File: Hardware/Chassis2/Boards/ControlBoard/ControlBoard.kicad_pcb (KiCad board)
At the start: 6 copper layers, 260 x 45 mm, 213 parts, among them IC1 MCP2221A-I_ST, IC2 MAX22530AWE+, IC3 ISO1042BDWVR, IC4 CY15B102Q-SXET, IC6 ISO1042BDWVR, J1 Conn_02x08_Counter_Clockwise, J10 Conn_02x03_Counter_Clockwise, J11 TBP01R2W-508-06BE, J12 Conn_02x08_Counter_Clockwise, J13 Conn_02x03_Counter_Clockwise, J14 Conn_01x10, J15 UJ32-C-H-G-DSMT-3-P24-TR, J2 Conn_01x02, J3 22-04-1041, J5 TBP02R2W-381-08BE, J6 22-04-1041, J7 Conn_02x08_Counter_Clockwise, J8 22-04-1041, J9 22-04-1041, U1 STM32H723ZGTx, U2 ISO1212, U3 LT3080xQ, U4 ISO1212, U5 ISO1212, U6 ISO1212, U7 BTS462TATMA1, U8 BTS462TATMA1, Y1 8MHz

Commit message: eod 2026-07-08
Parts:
- removed C1: ADCM-S05R5SA224XB, InverterCom:ADCMS05R5SA224XB
- removed C6: 100nF, Capacitor_SMD:C_1210_3225Metric_Pad1.33x2.70mm_HandSolder
- removed C7: 1uF, Capacitor_SMD:C_1210_3225Metric_Pad1.33x2.70mm_HandSolder
- removed IC1: MCP2221A-I_ST, InverterCom:SOP65P640X120-14N
- removed J15: UJ32-C-H-G-DSMT-3-P24-TR, InverterCom:UJ32CHGDSMT3P24TR
- removed JP1: Jumper_2_Small_Bridged, Jumper:SolderJumper-2_P1.3mm_Bridged_Pad1.0x1.5mm
- removed JP2: Jumper_2_Small_Open, Jumper:SolderJumper-2_P1.3mm_Open_RoundedPad1.0x1.5mm
- removed R13, R29, R30: 10k, Resistor_SMD:R_1210_3225Metric_Pad1.30x2.65mm_HandSolder
- removed R32, R33: 22, Resistor_SMD:R_1210_3225Metric_Pad1.30x2.65mm_HandSolder
- removed R34, R35, R36, R71, R72: 4.7k, Resistor_SMD:R_1210_3225Metric_Pad1.30x2.65mm_HandSolder
- removed TP24, TP25, TP26: TestPoint, TestPoint:TestPoint_Loop_D2.54mm_Drill1.5mm_Beaded
- added C147: 1uF, Capacitor_SMD:C_1210_3225Metric_Pad1.33x2.70mm_HandSolder, B.Cu at (100.5, 18.0)
- added C149: 100nF, Capacitor_SMD:C_1210_3225Metric_Pad1.33x2.70mm_HandSolder, B.Cu at (100.5, 25.0)
- added C197: 100nF, Capacitor_SMD:C_1210_3225Metric_Pad1.33x2.70mm_HandSolder, B.Cu at (105.5, 18.0)
- added C198: 10uF, Capacitor_SMD:C_1210_3225Metric_Pad1.33x2.70mm_HandSolder, B.Cu at (100.5, 21.5)
- added C200: 1uF, Capacitor_SMD:C_1210_3225Metric_Pad1.33x2.70mm_HandSolder, B.Cu at (105.5, 25.0)
- added C201: 100nF, Capacitor_SMD:C_1210_3225Metric_Pad1.33x2.70mm_HandSolder, B.Cu at (105.5, 21.5)
- added C202: 100nF, Capacitor_SMD:C_1210_3225Metric_Pad1.33x2.70mm_HandSolder, B.Cu at (135.0, 43.0)
- added C203: 100nF, Capacitor_SMD:C_1210_3225Metric_Pad1.33x2.70mm_HandSolder, B.Cu at (123.4, 43.0)
- added C208: 10uF, Capacitor_SMD:C_1210_3225Metric_Pad1.33x2.70mm_HandSolder, B.Cu at (146.9, 8.50)
- added C209: 10uF, Capacitor_SMD:C_1210_3225Metric_Pad1.33x2.70mm_HandSolder, B.Cu at (156.5, 9.56)
- added C210: 10uF, Capacitor_SMD:C_1210_3225Metric_Pad1.33x2.70mm_HandSolder, B.Cu at (166.4, 8.50)
- added C27: 100nF, Capacitor_SMD:C_1210_3225Metric_Pad1.33x2.70mm_HandSolder, B.Cu at (129.5, 39.5)
- added C28: 100nF, Capacitor_SMD:C_1210_3225Metric_Pad1.33x2.70mm_HandSolder, B.Cu at (141.5, 43.0)
- added C33: 22pF, Capacitor_SMD:C_1210_3225Metric_Pad1.33x2.70mm_HandSolder, B.Cu at (108.5, 6.00)
- added C48: 22pF, Capacitor_SMD:C_1210_3225Metric_Pad1.33x2.70mm_HandSolder, B.Cu at (103.5, 6.00)
- added IC5: ISO1042BDWVR, InverterCom:SOIC127P1150X280-8N, B.Cu at (65.0, 32.5)
- added IC7: ISO1042BDWVR, InverterCom:SOIC127P1150X280-8N, B.Cu at (65.5, 14.0)
- added J4: B2B-XH-AM_LF__SN_, InverterCom:B2BXHAMLFSN, F.Cu at (157.8, 3.98)
- added R87: 1k, Resistor_SMD:R_1210_3225Metric_Pad1.30x2.65mm_HandSolder, B.Cu at (220.6, 2.25)
- added R88: 10k, Resistor_SMD:R_1210_3225Metric_Pad1.30x2.65mm_HandSolder, B.Cu at (135.0, 39.5)
- added R89: 10k, Resistor_SMD:R_1210_3225Metric_Pad1.30x2.65mm_HandSolder, B.Cu at (123.5, 39.5)
- added R90: 10k, Resistor_SMD:R_1210_3225Metric_Pad1.30x2.65mm_HandSolder, B.Cu at (153.5, 3.00)
- added R91: 1k, Resistor_SMD:R_1210_3225Metric_Pad1.30x2.65mm_HandSolder, B.Cu at (152.0, 7.50)
- added R92: 10k, Resistor_SMD:R_1210_3225Metric_Pad1.30x2.65mm_HandSolder, B.Cu at (163.0, 3.05)
- added R93: 1k, Resistor_SMD:R_1210_3225Metric_Pad1.30x2.65mm_HandSolder, B.Cu at (161.0, 7.50)
- added R94: 10k, Resistor_SMD:R_1210_3225Metric_Pad1.30x2.65mm_HandSolder, B.Cu at (172.5, 3.00)
- added R95: 1k, Resistor_SMD:R_1210_3225Metric_Pad1.30x2.65mm_HandSolder, B.Cu at (171.6, 7.50)
- added U9: STM32G474RCTx, Package_QFP:LQFP-64_10x10mm_P0.5mm, F.Cu at (102.8, 21.7)
- added Y2: 8MHz, Crystal:Crystal_HC49-4H_Vertical, F.Cu at (108.4, 10.0)
- added Z5: MM3Z3V0ST1G, InverterCom:SOD2512X100N, B.Cu at (149.5, 1.50)
- added Z6: MM3Z3V0ST1G, InverterCom:SOD2512X100N, B.Cu at (159.0, 1.50)
- added Z7: MM3Z3V0ST1G, InverterCom:SOD2512X100N, B.Cu at (168.5, 1.50)
- J1: value Conn_02x08_Counter_Clockwise -> B2B-XH-AM_LF__SN_; footprint Connector_PinHeader_2.54mm:PinHeader_2x08_P2.54mm_Vertical -> InverterCom:B2BXHAMLFSN
- J14: value Conn_01x10 -> Conn_02x08_Counter_Clockwise; footprint Connector_PinHeader_2.54mm:PinHeader_1x10_P2.54mm_Vertical -> Connector_PinHeader_2.54mm:PinHeader_2x08_P2.54mm_Vertical
- J2: value Conn_01x02 -> Conn_02x10_Counter_Clockwise; footprint Connector_PinHeader_2.54mm:PinHeader_1x02_P2.54mm_Vertical -> Connector_PinSocket_2.54mm:PinSocket_2x10_P2.54mm_Vertical
- J5: value TBP02R2W-381-08BE -> B2B-XH-AM_LF__SN_; footprint InverterCom:TBP02R2W38108BE -> InverterCom:B2BXHAMLFSN
- R31: moved to B.Cu
- U3: footprint Package_TO_SOT_SMD:TO-263-5_TabPin3 -> Package_TO_SOT_SMD:TO-263-5_TabPin6
- moved J2 151.1 mm to (95.4, 40.0), turned to 90 degrees
- moved C30 66.5 mm to (118.0, 3.25), turned to 180 degrees
- moved J5 66.2 mm to (167.2, 3.98), turned to 180 degrees
- moved C192 53.3 mm to (123.7, 15.8), turned to 90 degrees
- moved Y1 52.6 mm to (126.2, 4.50), turned to 180 degrees
- moved C26 51.5 mm to (129.5, 2.50), turned to 0 degrees
- moved C184 50.5 mm to (124.4, 30.6)
- moved IC4 49.3 mm to (137.8, 3.37), turned to 180 degrees
- moved C135 49.0 mm to (129.5, 20.0)
- moved C194 45.0 mm to (135.9, 29.6), turned to -90 degrees
- moved J1 44.8 mm to (148.2, 3.98), turned to 180 degrees
- moved C182 43.8 mm to (124.4, 27.1), turned to 180 degrees
- moved C134 43.7 mm to (124.3, 23.6), turned to 0 degrees
- moved LED2 43.4 mm to (146.5, 42.5), turned to 90 degrees
- moved C136 43.1 mm to (128.7, 24.2), turned to 90 degrees
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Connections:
- net /ADC/SPI_RX_A renamed /ADC/SPI_MISO_A
- net /ADC/SPI_TX_A renamed /ADC/SPI_MOSI_A
- net /CAN Transciever/CAN_RX renamed /CAN Transciever/A_CAN_RX
- net /CAN Transciever/CAN_TX renamed /CAN Transciever/A_CAN_TX
- net /CAN Transciever1/CAN_RX renamed /CAN Transciever1/A_CAN_RX
- net /CAN Transciever1/CAN_TX renamed /CAN Transciever1/A_CAN_TX
- net /Control/DC_LINK_CURRENT_SENSE renamed /Control/SN_CUR_SENSE_DC_LINK_SIG
- net /Control/DC_LINK_CURRENT_SENSE_REF renamed /Control/SN_CUR_SENSE_DC_LINK_REF
- net /Control/DEBUG_NJTRST renamed /Control/MP_DEBUG_NJTRST
- net /Control/DEBUG_TRGIO renamed /Control/MP_DEBUG_TRGIO
- net /Control/FRAM_CS renamed /Control/Main Processor/FRAM_CS
- net /Control/FRAM_HOLD renamed /Control/Main Processor/FRAM_HOLD
- net /Control/FRAM_SPI_MISO renamed /Control/Main Processor/FRAM_SPI_MISO
- net /Control/FRAM_SPI_MOSI renamed /Control/Main Processor/FRAM_SPI_MOSI
- net /Control/FRAM_SPI_SCK renamed /Control/Main Processor/FRAM_SPI_SCK
- net /Control/FRAM_WP renamed /Control/Main Processor/FRAM_WP
- net /Control/HALL_U_ENCODER_SIN renamed /Control/SN_HALL_U_ENCODER_SIN
- net /Control/HALL_V_ENCODER_COS renamed /Control/SN_HALL_V_ENCODER_COS
- net /Control/HALL_W renamed /Control/SN_HALL_W
- net /Control/MOTOR_TEMP renamed /Control/SN_MOTOR_TEMP
- net /Control/PHASE_U_CURRENT_SENSE renamed /Control/SN_CUR_SENSE_PH_U_SIG
- net /Control/PHASE_U_CURRENT_SENSE_REF renamed /Control/SN_CUR_SENSE_PH_U_REF
- net /Control/PHASE_V_CURRENT_SENSE renamed /Control/SN_CUR_SENSE_PH_V_SIG
- net /Control/PHASE_V_CURRENT_SENSE_REF renamed /Control/SN_CUR_SENSE_PH_V_REF
- net /Control/PHASE_W_CURRENT_SENSE renamed /Control/SN_CUR_SENSE_PH_W_SIG
- net /Control/PHASE_W_CURRENT_SENSE_REF renamed /Control/SN_CUR_SENSE_PH_W_REF
- net /Control/THROTTLE_A renamed /Control/SN_THROTTLE_A
- net /Control/USER_DIN_1 renamed /Control/SN_USER_DIN_1
- net /Control/USER_DIN_2 renamed /Control/SN_USER_DIN_2
- net /Control/USER_DIN_3 renamed /Control/SN_USER_DIN_3
- net /Control/USER_DIN_4 renamed /Control/SN_USER_DIN_4
- net /Control/USER_DIN_5 renamed /Control/MP_USER_DIN_5
- net /Control/USER_DIN_6 renamed /Control/MP_USER_DIN_6
- net /Control/USER_DIN_7 renamed /Control/MP_USER_DIN_7
- net /Control/USER_DIN_8 renamed /Control/MP_USER_DIN_8
- net /SWCLK renamed /MP_SWCLK
- net /VSENSE_DC_LINK_Y renamed /VS_DC_LINK_Y
- net /VSENSE_GND_Y renamed /VS_GND_Y
- net /VSENSE_PH_U_Y renamed /VS_PH_U_Y
- net /VSENSE_PH_V_Y renamed /VS_PH_V_Y
- net /VSENSE_PH_W_Y renamed /VS_PH_W_Y
- net Net-(IC3-CANH) renamed /CAN Transciever1/CAN_H
- net Net-(IC3-CANL) renamed /CAN Transciever1/CAN_L
- net Net-(IC6-CANH) renamed /CAN Transciever/CAN_H
- net Net-(IC6-CANL) renamed /CAN Transciever/CAN_L
- C134 pad 1: Net-(C1-+) -> /+3.3V_A
- C135 pad 1: /+3.3V_A -> /GND_A
- C135 pad 2: Net-(U1-VDDA) -> /+3.3V_A
- C136 pad 1: /+3.3V_A -> /GND_A
- C136 pad 2: Net-(U1-VDDA) -> /+3.3V_A
- C140 pad 2: /ANALOG_GND -> /GND_A
- C141 pad 2: /ANALOG_GND -> /GND_A
- C142 pad 1: /ANALOG_GND -> /GND_A
- C143 pad 2: /ANALOG_GND -> /GND_A
- C144 pad 2: /ANALOG_GND -> /GND_A
- C145 pad 2: /ANALOG_GND -> /GND_A
- C146 pad 2: /ANALOG_GND -> /GND_A
- C190 pad 2: /GND_A -> Net-(C190-Pad2)
- C191 pad 2: /GND_A -> Net-(C190-Pad2)
- C192 pad 1: Net-(U1-VREF+) -> /+3.3V_A
- C193 pad 1: Net-(U1-VREF+) -> /+3.3V_A
- C21 pad 2: /ANALOG_GND -> /GND_A
- C22 pad 2: /ANALOG_GND -> /GND_A
- C23 pad 2: /ANALOG_GND -> /GND_A
- C24 pad 2: /ANALOG_GND -> /GND_A
- C25 pad 2: /ANALOG_GND -> /GND_A
- C29 pad 2: /ANALOG_GND -> /GND_A
- C38 pad 2: /ANALOG_GND -> /GND_A
- C39 pad 2: /ANALOG_GND -> /GND_A
- C42 pad 2: /ANALOG_GND -> /GND_A
- C43 pad 2: /ANALOG_GND -> /GND_A
- C44 pad 2: /ANALOG_GND -> /GND_A
- C45 pad 1: /Control/THROTTLE_B -> /Control/SN_THROTTLE_B
- C45 pad 2: /ANALOG_GND -> /GND_A
- C46 pad 2: /ANALOG_GND -> /GND_A
- C47 pad 2: /ANALOG_GND -> /GND_A
- J1 pad 2: /FAULT -> Net-(Z5-K)
- J14 pad 1: /+3.3V_A -> /GND_A
- J14 pad 10: /RESET -> /+3.3V_A
- J14 pad 2: /SWDIO -> /MP_SWO
- J14 pad 3: /GND_A -> /MP_BOOTSEL
- J14 pad 5: /GND_A -> /MP_SWDIO
- J14 pad 6: /SWO -> /MP_RESET
- J14 pad 7: unconnected-(J14-Pin_7-Pad7) -> /GND_A
- J14 pad 8: unconnected-(J14-Pin_8-Pad8) -> /USB_DP
- J14 pad 9: /GND_A -> /USB_DM
- J2 pad 1: /+12V_A -> /GND_A
- J2 pad 2: /GND_A -> /FAULT
- J3 pad 3: /ANALOG_GND -> /GND_A
- J5 pad 1: /+3.3V_A -> /GND_A
- J5 pad 2: /HS_TMP_2 -> Net-(Z7-K)
- J6 pad 3: /ANALOG_GND -> /GND_A
- J8 pad 3: /ANALOG_GND -> /GND_A
- J9 pad 3: /ANALOG_GND -> /GND_A
- R14 pad 1: /BOOTSEL -> /MP_BOOTSEL
- R40 pad 1: /ANALOG_GND -> /GND_A
- R42 pad 1: /ANALOG_GND -> /GND_A
- R44 pad 1: /ANALOG_GND -> /GND_A
- R46 pad 1: /ANALOG_GND -> /GND_A
- R48 pad 1: /ANALOG_GND -> /GND_A
- R50 pad 1: /ANALOG_GND -> /GND_A
- R52 pad 1: /ANALOG_GND -> /GND_A
- R54 pad 1: /ANALOG_GND -> /GND_A
- R56 pad 1: /ANALOG_GND -> /GND_A
- R58 pad 1: /ANALOG_GND -> /GND_A
- R60 pad 1: /ANALOG_GND -> /GND_A
- R61 pad 1: /Control/THROTTLE_B -> /Control/SN_THROTTLE_B
- R62 pad 1: /ANALOG_GND -> /GND_A
- R62 pad 2: /Control/THROTTLE_B -> /Control/SN_THROTTLE_B
- R64 pad 1: /ANALOG_GND -> /GND_A
- R66 pad 1: /ANALOG_GND -> /GND_A
- R70 pad 1: /RESET -> /MP_RESET
- R86 pad 1: /ANALOG_GND -> /GND_A
- S1 pad 3: /BOOTSEL -> /MP_BOOTSEL
- S1 pad 4: /BOOTSEL -> /CP_BOOTSEL
- S2 pad 3: /RESET -> /MP_RESET
- S2 pad 4: /RESET -> /CP_RESET
- U1 pad 105: /SWDIO -> /MP_SWDIO
- U1 pad 111: /GATE_DRIVE_PWR_ENABLE -> /GATE_DRIVE_PWR1_ENABLE
- U1 pad 117: unconnected-(U1-PD3-Pad117) -> /GATE_DRIVE_PWR2_FB
- U1 pad 118: unconnected-(U1-PD4-Pad118) -> /GATE_DRIVE_PWR1_FB
- U1 pad 133: /SWO -> /MP_SWO
- U1 pad 138: /BOOTSEL -> /MP_BOOTSEL
- U1 pad 18: unconnected-(U1-PF6-Pad18) -> /Control/SN_THROTTLE_B
- U1 pad 20: unconnected-(U1-PF8-Pad20) -> /HS_TMP_1
- U1 pad 25: /RESET -> /MP_RESET
- U1 pad 31: /ANALOG_GND -> /GND_A
- U1 pad 32: Net-(U1-VREF+) -> /+3.3V_A
- U1 pad 33: Net-(U1-VDDA) -> /+3.3V_A
- U1 pad 40: /Control/THROTTLE_B -> /Control/PHASE_CURSENSE_COMP_N
- U1 pad 41: /HS_TMP_1 -> /Control/DC_LINK_CURSENSE_COMP_N
- U1 pad 6: Net-(C1-+) -> /+3.3V_A
- U1 pad 69: /Control/USART3_TX -> /Control/Main Processor/USART3_TX
- U1 pad 70: /Control/USART3_RX -> /Control/Main Processor/USART3_RX
- U1 pad 77: unconnected-(U1-PD8-Pad77) -> /Control/Main Processor/COPROCESSOR_SYNC
- U1 pad 78: unconnected-(U1-PD9-Pad78) -> /Control/Main Processor/COPROCESSOR_WAKEUP
- U1 pad 79: unconnected-(U1-PD10-Pad79) -> /CP_RESET
- U1 pad 80: unconnected-(U1-PD11-Pad80) -> /CP_BOOTSEL
- U1 pad 96: unconnected-(U1-PC6-Pad96) -> /Control/Main Processor/COPROCESSOR_TIMER_SYNC_OUT
- U3 pad 5: Net-(U3-IN) -> /+12V_SWITCHED_A
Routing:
- net /ANALOG_GND: track 127.5 -> 0.00 mm, vias 13 -> 0
- net /RESET: track 120.4 -> 0.00 mm, vias 7 -> 0
- net /CAN Transciever1/A_CAN_TX: track 116.3 -> 22.0 mm, vias 2 -> 0
- net /ADC/ADC1_CS_A: track 122.0 -> 31.1 mm, vias 2 -> 0
- net /BOOTSEL: track 90.5 -> 0.00 mm, vias 5 -> 0
- net /ADC/ADC1_INT_A: track 121.4 -> 31.1 mm, vias 2 -> 0
- net /FAULT: track 90.1 -> 0.00 mm, vias 4 -> 0
- net /CAN Transciever/A_CAN_TX: track 100.4 -> 20.1 mm, vias 2 -> 0
- net /CAN Transciever1/A_CAN_RX: track 103.9 -> 23.9 mm, vias 4 -> 0
- net /CAN Transciever/A_CAN_RX: track 97.8 -> 18.4 mm, vias 2 -> 0
- net /Control/USART3_TX: track 75.2 -> 0.00 mm, vias 2 -> 0
- net /ADC/SPI_MISO_A: track 104.8 -> 31.9 mm, vias 2 -> 0
- net /ADC/SPI_MOSI_A: track 103.5 -> 31.4 mm, vias 2 -> 0
- net /Control/SN_USER_DIN_1: track 105.2 -> 33.3 mm, vias 3 -> 0
- net /Control/USART3_RX: track 71.3 -> 0.00 mm, vias 2 -> 0
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- removed copper zone on B.Cu, net /ANALOG_GND
- removed copper zone on F.Cu, net /ANALOG_GND
- removed copper zone on In1.Cu, net /ANALOG_GND
- removed copper zone on In4.Cu, net /ANALOG_GND
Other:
- board text removed: "3.3V|TMP2|3.3V|TMP3|GND|3.3V|TMP1|GND"

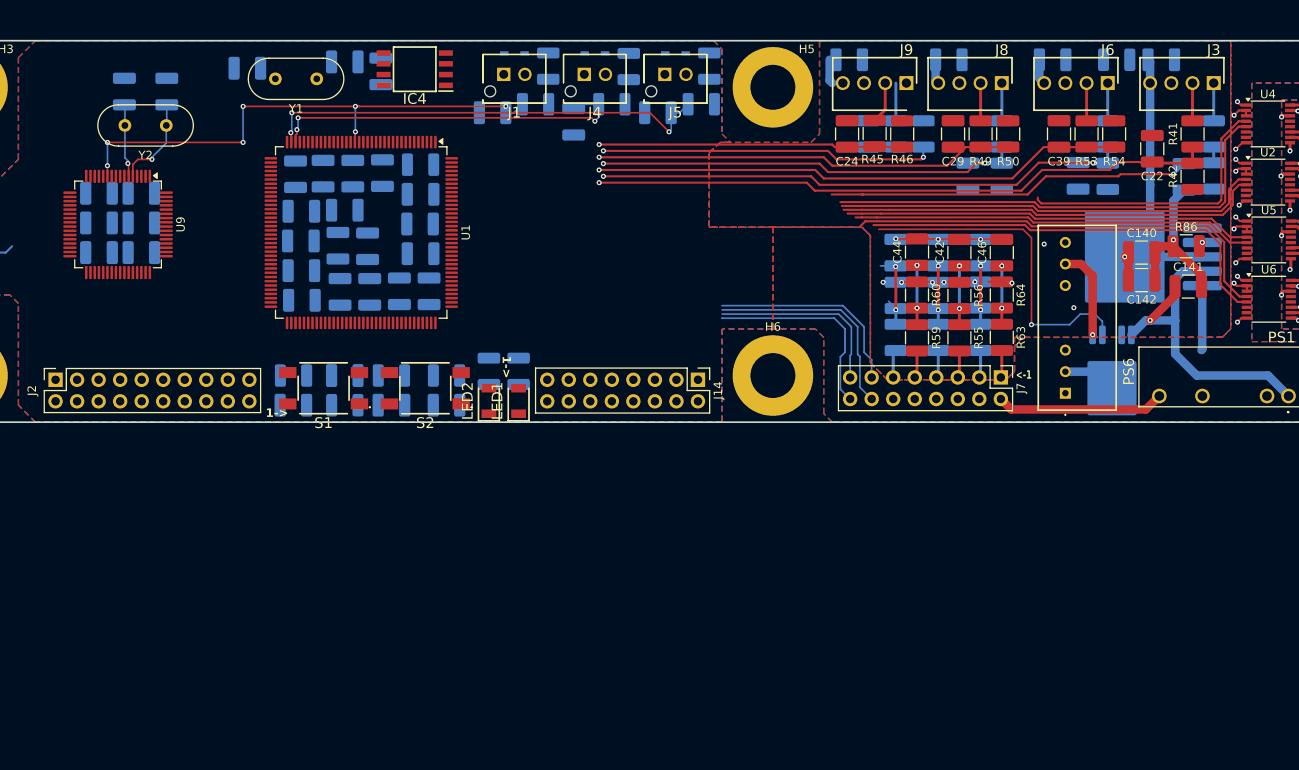
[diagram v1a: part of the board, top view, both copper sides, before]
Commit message: Add Supervisory power ic
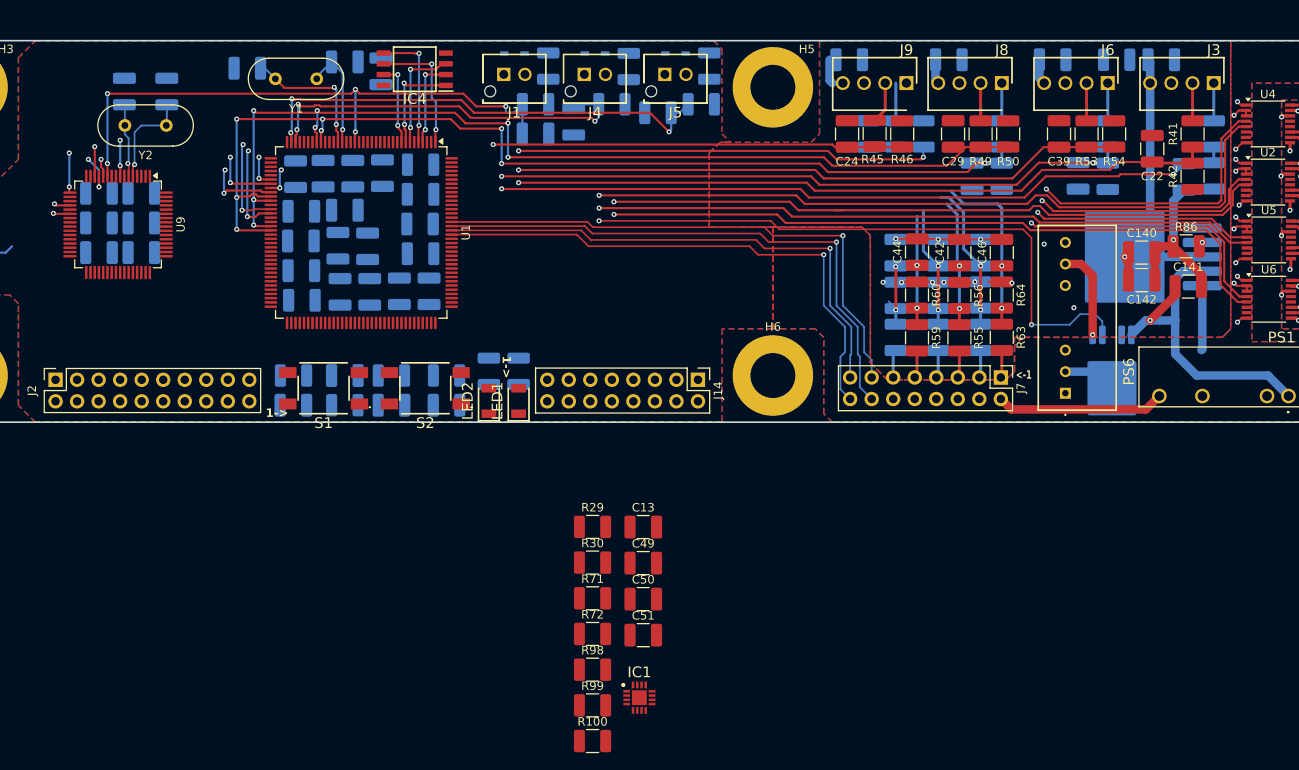
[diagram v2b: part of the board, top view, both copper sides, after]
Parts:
- added C13: 100nF, Capacitor_SMD:C_1210_3225Metric_Pad1.33x2.70mm_HandSolder, F.Cu at (164.7, 57.4)
- added C49: 10nF, Capacitor_SMD:C_1210_3225Metric_Pad1.33x2.70mm_HandSolder, F.Cu at (164.7, 61.6)
- added C50: 10nF, Capacitor_SMD:C_1210_3225Metric_Pad1.33x2.70mm_HandSolder, F.Cu at (164.7, 65.9)
- added C51: 10nF, Capacitor_SMD:C_1210_3225Metric_Pad1.33x2.70mm_HandSolder, F.Cu at (164.7, 70.1)
- added IC1: TPS389006ADJRTER, InverterCom:QFN50P300X300X80-17N-D, F.Cu at (164.2, 77.5)
- added R100: 20k, Resistor_SMD:R_1210_3225Metric_Pad1.30x2.65mm_HandSolder, F.Cu at (158.7, 82.6)
- added R29: 3k, Resistor_SMD:R_1210_3225Metric_Pad1.30x2.65mm_HandSolder, F.Cu at (158.7, 57.4)
- added R30: 1k, Resistor_SMD:R_1210_3225Metric_Pad1.30x2.65mm_HandSolder, F.Cu at (158.7, 61.6)
- added R71: 10k, Resistor_SMD:R_1210_3225Metric_Pad1.30x2.65mm_HandSolder, F.Cu at (158.7, 65.8)
- added R72: 20k, Resistor_SMD:R_1210_3225Metric_Pad1.30x2.65mm_HandSolder, F.Cu at (158.7, 70.0)
- added R98: 10k, Resistor_SMD:R_1210_3225Metric_Pad1.30x2.65mm_HandSolder, F.Cu at (158.7, 74.2)
- added R99: 10k, Resistor_SMD:R_1210_3225Metric_Pad1.30x2.65mm_HandSolder, F.Cu at (158.7, 78.4)
- moved C208 5.65 mm to (152.0, 11.0), turned to 0 degrees
- moved C25 0.50 mm to (203.5, 16.0)
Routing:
- net /Control/SN_CUR_SENSE_PH_U_REF: track 48.6 -> 152.7 mm, vias 1 -> 6
- net /Control/SN_CUR_SENSE_PH_W_SIG: track 51.1 -> 143.6 mm, vias 1 -> 8
- net /Control/SN_CUR_SENSE_DC_LINK_SIG: track 39.9 -> 117.7 mm, vias 1 -> 4
- net /Control/SN_CUR_SENSE_PH_V_REF: track 64.7 -> 141.3 mm, vias 2 -> 6
- net /Control/SN_CUR_SENSE_DC_LINK_REF: track 46.0 -> 118.5 mm, vias 2 -> 6
- net /Control/SN_CUR_SENSE_PH_W_REF: track 51.8 -> 123.8 mm, vias 2 -> 8
- net /Control/SN_CUR_SENSE_PH_V_SIG: track 64.5 -> 132.5 mm, vias 1 -> 4
- net /Control/SN_CUR_SENSE_PH_U_SIG: track 74.9 -> 140.3 mm, vias 1 -> 4
- net /Control/SN_USER_DIN_1: track 33.3 -> 83.8 mm, vias 0 -> 1
- net /DOUT1_A: track 24.1 -> 65.0 mm, vias 0 -> 1
- net /DOUT2_A: track 26.0 -> 66.4 mm, vias 0 -> 1
- net /DOUT3_A: track 21.9 -> 61.8 mm, vias 0 -> 1
- net /DOUT4_A: track 24.0 -> 63.6 mm, vias 0 -> 1
- net /ONBOARD_12V_ENABLE_A: track 39.5 -> 72.9 mm, vias 1 -> 2
- net /Control/MP_USER_DIN_8: track 50.6 -> 81.7 mm, vias 0 -> 1
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
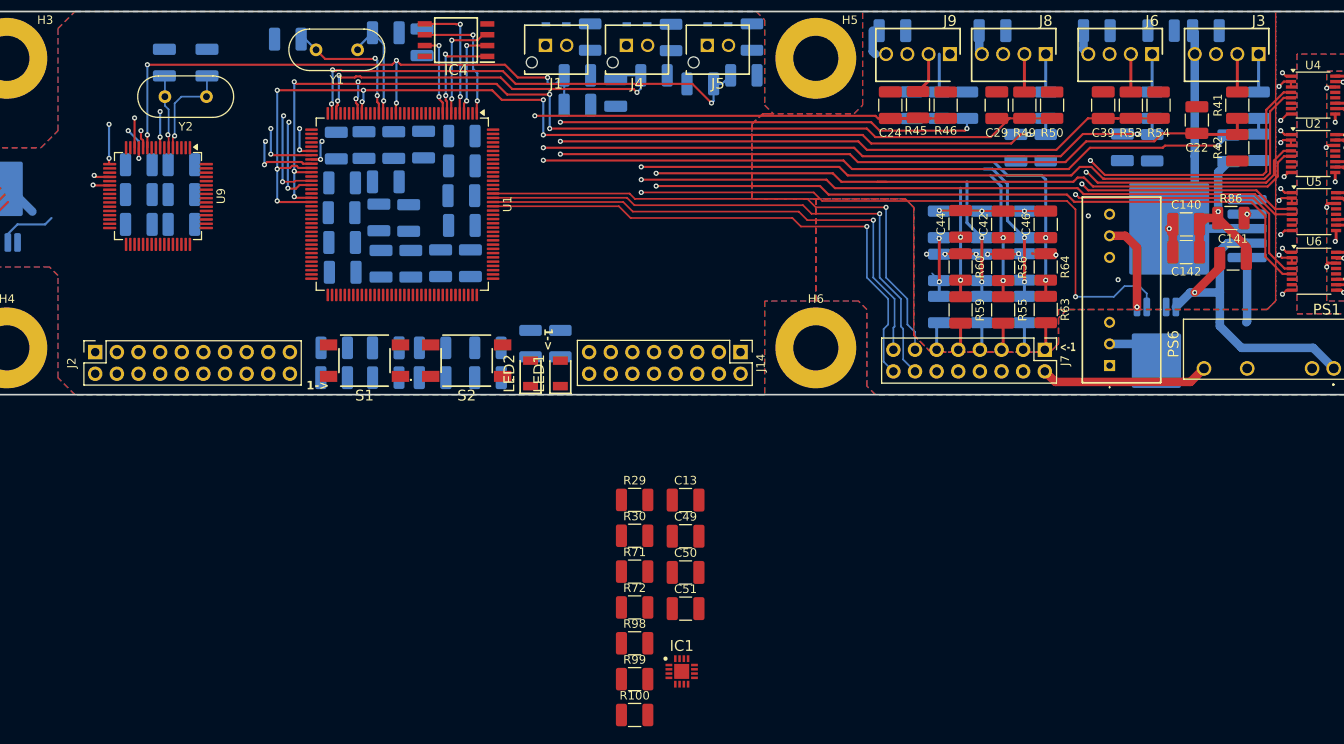
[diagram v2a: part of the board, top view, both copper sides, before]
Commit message: Add Schematic / Controlboard Support for Multi-Drive Mulit-Phase, DDCP
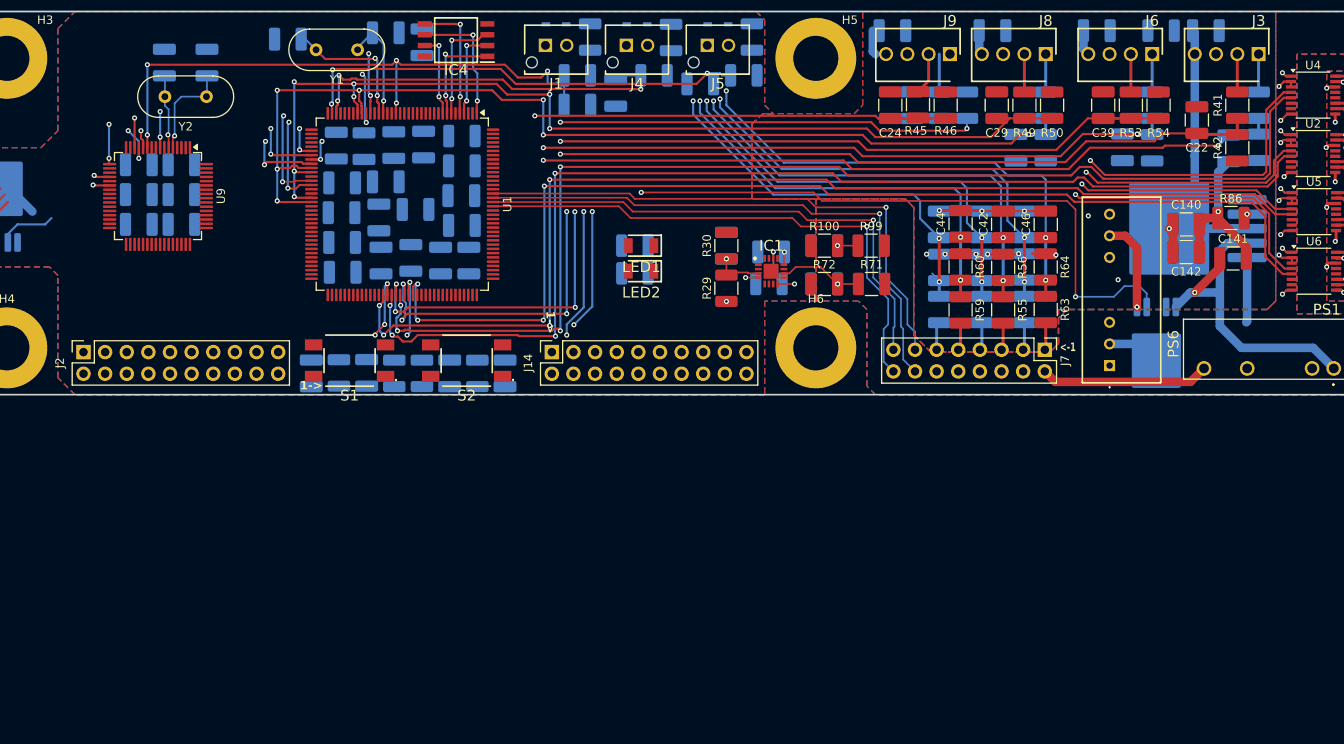
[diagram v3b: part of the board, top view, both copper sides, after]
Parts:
- C13, C49, C50, C51, R98: moved to B.Cu
- J14: value Conn_02x08_Counter_Clockwise -> Conn_02x10_Counter_Clockwise; footprint Connector_PinHeader_2.54mm:PinHeader_2x08_P2.54mm_Vertical -> Connector_PinSocket_2.54mm:PinSocket_2x10_P2.54mm_Vertical
- moved R100 59.4 mm to (181.0, 27.5)
- moved R99 58.0 mm to (186.5, 27.5)
- moved IC1 48.2 mm to (174.8, 30.5)
- moved R98 45.0 mm to (174.5, 32.0)
- moved R72 44.0 mm to (181.0, 32.0)
- moved R71 43.8 mm to (186.6, 32.0)
- moved C51 42.9 mm to (169.5, 27.5), turned to 90 degrees
- moved C50 41.7 mm to (181.0, 27.5), turned to 180 degrees
- moved R30 35.7 mm to (169.5, 27.5), turned to 90 degrees
- moved C49 33.8 mm to (181.0, 32.0), turned to 180 degrees
- moved C13 30.8 mm to (174.8, 28.2), turned to 180 degrees
- moved R29 27.1 mm to (169.5, 32.5), turned to 90 degrees
- moved J14 22.2 mm to (149.0, 40.0), turned to 90 degrees
- moved LED1 17.8 mm to (159.5, 27.5), turned to 180 degrees
- moved LED2 17.7 mm to (159.5, 30.5), turned to 180 degrees
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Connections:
- C13 pad 1: /Control/Power Supply Monitor/+3.3V_A -> /+3.3V_A
- C13 pad 2: /Control/Power Supply Monitor/GND_A -> /GND_A
- C140 pad 1: /Current Sensors/CURRENT_SENSE_+5V_A -> /+5V_ISENSE_A
- C142 pad 2: /Current Sensors/CURRENT_SENSE_+5V_A -> /+5V_ISENSE_A
- C143 pad 1: /Current Sensors/CURRENT_SENSE_+5V_A -> /+5V_ISENSE_A
- C144 pad 1: /Current Sensors/CURRENT_SENSE_+5V_A -> /+5V_ISENSE_A
- C145 pad 1: /Current Sensors/CURRENT_SENSE_+5V_A -> /+5V_ISENSE_A
- C146 pad 1: /Current Sensors/CURRENT_SENSE_+5V_A -> /+5V_ISENSE_A
- C49 pad 2: /Control/Power Supply Monitor/GND -> /GND_A
- C50 pad 2: /Control/Power Supply Monitor/GND -> /GND_A
- C51 pad 2: /Control/Power Supply Monitor/GND -> /GND_A
- IC1 pad 1: /Control/Power Supply Monitor/GATE_DRIVER_PWR2_FEEDBACK -> /GATE_DRIVE_PWR2_FEEDBACK
- IC1 pad 12: /Control/Power Supply Monitor/+3.3V_A -> /+3.3V_A
- IC1 pad 15: /Control/Power Supply Monitor/SDA -> /Control/Main Processor/VOLTAGE_MONITOR_I2C_SDA
- IC1 pad 16: /Control/Power Supply Monitor/SCL -> /Control/Main Processor/VOLTAGE_MONITOR_I2C_SCL
- IC1 pad 17: /Control/Power Supply Monitor/GND_A -> /GND_A
- IC1 pad 2: /Control/Power Supply Monitor/GATE_DRIVER_PWR1_FEEDBACK -> /GATE_DRIVE_PWR1_FEEDBACK
- IC1 pad 6: /Control/Power Supply Monitor/GND_A -> /GND_A
- IC1 pad 8: /Control/Power Supply Monitor/+3.3V_A -> /+3.3V_A
- J14 pad 10: /+3.3V_A -> /MD_FIBER_RX
- J14 pad 11: /CP_RESET -> /FAULT
- J14 pad 12: /CP_SWDIO -> /MD_FIBER_SYNC
- J14 pad 13: /CP_SWCLK -> /USB_DM
- J14 pad 14: /CP_BOOTSEL -> /+3.3V_A
- J14 pad 15: /GND_A -> /CP_RESET
- J14 pad 16: /+12V_A -> /CP_SWDIO
- J14 pad 9: /USB_DM -> /MD_FIBER_TX
- J3 pad 4: /Current Sensors/CURRENT_SENSE_+5V_A -> /+5V_ISENSE_A
- J6 pad 4: /Current Sensors/CURRENT_SENSE_+5V_A -> /+5V_ISENSE_A
- J8 pad 4: /Current Sensors/CURRENT_SENSE_+5V_A -> /+5V_ISENSE_A
- J9 pad 4: /Current Sensors/CURRENT_SENSE_+5V_A -> /+5V_ISENSE_A
- R100 pad 1: /Control/Power Supply Monitor/GND -> /GND_A
- R29 pad 1: /Control/Power Supply Monitor/+12V_A -> /+12V_A
- R30 pad 2: /Control/Power Supply Monitor/GND -> /GND_A
- R71 pad 2: /Control/Power Supply Monitor/+5V_A -> /+5V_A
- R72 pad 1: /Control/Power Supply Monitor/GND -> /GND_A
- R87 pad 2: /Current Sensors/CURRENT_SENSE_+5V_A -> /+5V_ISENSE_A
- R98 pad 1: /Control/Power Supply Monitor/GND_A -> /GND_A
- R99 pad 2: /Control/Power Supply Monitor/+5V_ISENSE_A -> /+5V_ISENSE_A
- U1 pad 114: unconnected-(U1-PD0-Pad114) -> /MD_FIBER_RX
- U1 pad 117: /GATE_DRIVE_PWR2_FB -> /GATE_DRIVE_PWR2_FEEDBACK
- U1 pad 118: /GATE_DRIVE_PWR1_FB -> /GATE_DRIVE_PWR1_FEEDBACK
- U1 pad 140: unconnected-(U1-PB9-Pad140) -> /MD_FIBER_TX
- U1 pad 55: unconnected-(U1-PF15-Pad55) -> /Control/Main Processor/VOLTAGE_MONITOR_I2C_SDA
- U1 pad 58: unconnected-(U1-PE7-Pad58) -> /MD_FIBER_SYNC
- U1 pad 81: unconnected-(U1-PD12-Pad81) -> /Control/Main Processor/VOLTAGE_MONITOR_I2C_SCL
- U3 pad 3: /Current Sensors/CURRENT_SENSE_+5V_A -> /+5V_ISENSE_A
- U3 pad 6: /Current Sensors/CURRENT_SENSE_+5V_A -> /+5V_ISENSE_A
- U9 pad 3: /GATE_DRIVE_PWR1_FB -> /GATE_DRIVE_PWR1_FEEDBACK
- U9 pad 4: /GATE_DRIVE_PWR2_FB -> /GATE_DRIVE_PWR2_FEEDBACK
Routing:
- net /Current Sensors/CURRENT_SENSE_+5V_A: track 98.2 -> 0.00 mm, vias 1 -> 0
- net /+5V_ISENSE_A: track 0.00 -> 98.2 mm, vias 0 -> 1
- net /Control/SN_HALL_U_ENCODER_SIN: track 20.5 -> 109.0 mm, vias 2 -> 5
- net /Control/SN_HALL_V_ENCODER_COS: track 17.8 -> 103.5 mm, vias 2 -> 5
- net /Control/MP_USER_DIN_5: track 75.9 -> 135.5 mm, vias 1 -> 6
- net /Control/SN_USER_DIN_4: track 79.1 -> 134.8 mm, vias 1 -> 4
- net /Control/MP_USER_DIN_7: track 79.9 -> 134.8 mm, vias 1 -> 5
- net /Control/SN_USER_DIN_1: track 83.8 -> 138.1 mm, vias 1 -> 5
- net /Control/MP_USER_DIN_6: track 78.1 -> 131.0 mm, vias 1 -> 4
- net /Control/SN_USER_DIN_2: track 85.9 -> 138.6 mm, vias 1 -> 4
- net /Control/SN_USER_DIN_3: track 77.3 -> 129.4 mm, vias 1 -> 5
- net /Control/MP_USER_DIN_8: track 81.7 -> 131.5 mm, vias 1 -> 4
- net /Control/SN_HALL_W: track 14.9 -> 56.9 mm, vias 2 -> 3
- net /Control/SN_THROTTLE_B: track 8.16 -> 47.2 mm, vias 2 -> 3
- net /Control/SN_MOTOR_TEMP: track 14.3 -> 52.4 mm, vias 2 -> 3
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
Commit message: Update README, Implement Powermon
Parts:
- moved Y2 0.50 mm to (108.4, 9.50)
- moved C186 0.20 mm to (130.2, 15.8)
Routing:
- net /Control/SN_MOTOR_TEMP: track 52.4 -> 140.9 mm, vias 3 -> 6
- net /Control/SN_HALL_W: track 56.9 -> 144.2 mm, vias 3 -> 7
- net /Control/SN_THROTTLE_A: track 50.2 -> 127.1 mm, vias 3 -> 7
- net /Control/SN_HALL_U_ENCODER_SIN: track 109.0 -> 155.2 mm, vias 5 -> 8
- net /Control/SN_THROTTLE_B: track 47.2 -> 87.7 mm, vias 3 -> 5
- net Net-(U1-PH1): track 16.3 -> 17.3 mm
